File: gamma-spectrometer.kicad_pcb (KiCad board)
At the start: 2 copper layers, 123.5 x 55 mm, 80 parts, among them J1 *, J2 *, J3 *, J4 *, J5 *, J6 *, Q1 2N7002, Q2 2N7002, Q3 MMBT5088LT1G, Q4 MMBT5088LT1G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

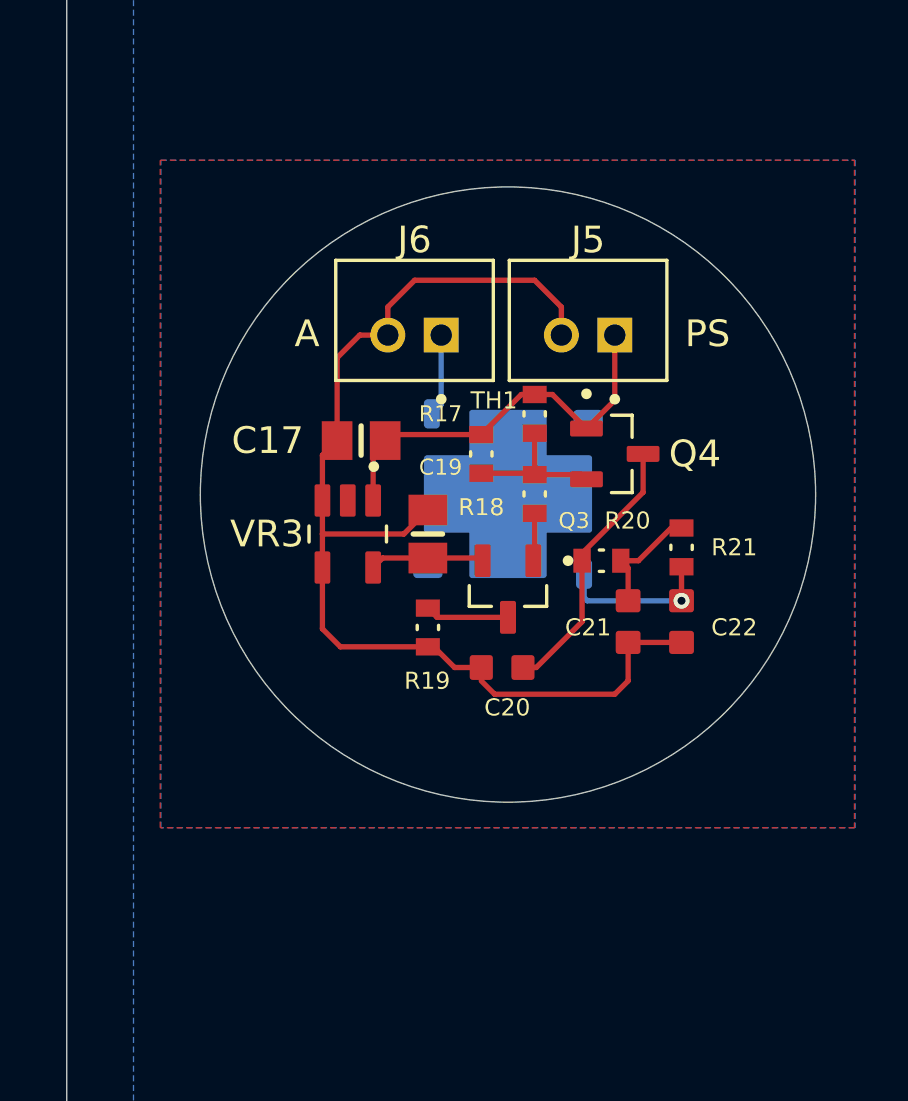
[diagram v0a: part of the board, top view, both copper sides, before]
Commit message: Corrected labels
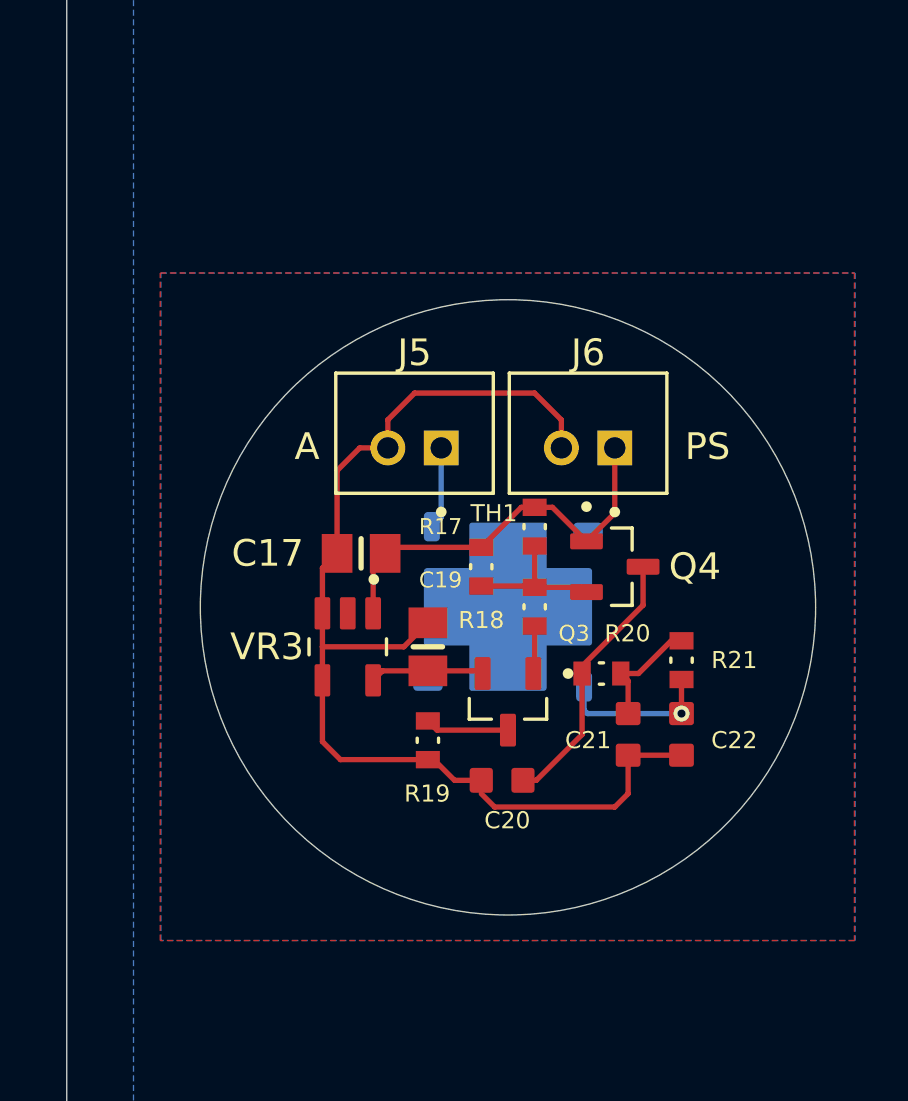
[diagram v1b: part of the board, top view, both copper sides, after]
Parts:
- moved C17 4.22 mm to (194.5, 82.2)
- moved C19 4.22 mm to (197.0, 85.7)
- moved C20 4.22 mm to (199.8, 90.7)
- moved C21 4.22 mm to (204.5, 89.0)
- moved C22 4.22 mm to (206.5, 89.0)
- moved J5 4.22 mm to (196.5, 77.7)
- moved J6 4.22 mm to (203.0, 77.7)
- moved Q3 4.22 mm to (200.0, 87.8)
- moved Q4 4.22 mm to (204.0, 82.7)
- moved R17 4.22 mm to (199.0, 82.7)
- moved R18 4.22 mm to (201.0, 84.2)
- moved R19 4.22 mm to (197.0, 89.2)
- moved R20 4.22 mm to (203.5, 86.7)
- moved R21 4.22 mm to (206.5, 86.2)
- moved TH1 4.22 mm to (201.0, 81.2)
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- renumbered J6 to J5, J5 to J6
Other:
- outline, holes or cut-outs redrawn

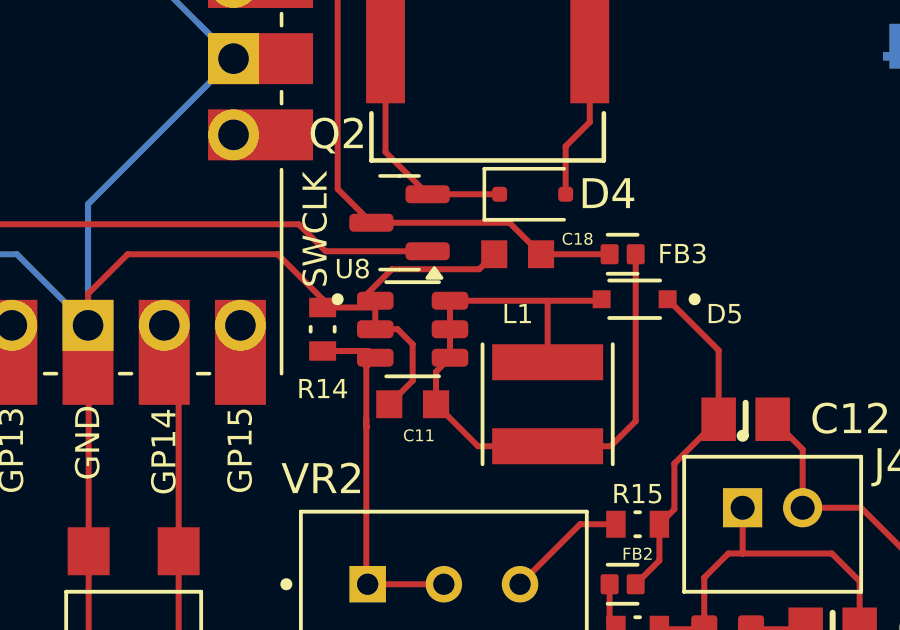
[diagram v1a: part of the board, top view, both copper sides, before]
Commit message: U8 5-6 pins connection error fix
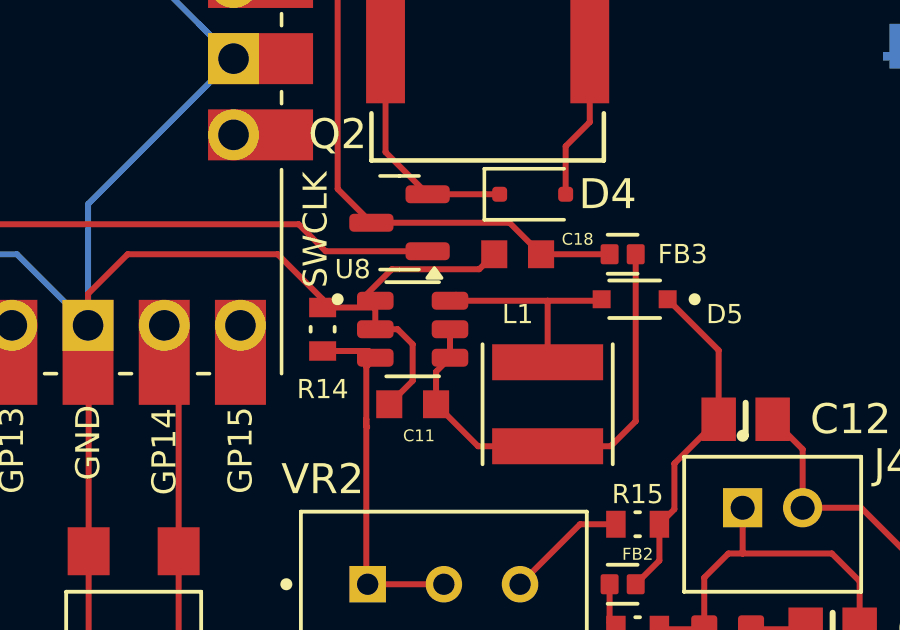
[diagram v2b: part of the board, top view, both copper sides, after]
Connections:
- C11 pad 1: Net-(D5-A) -> Net-(U8-VCC)
- FB3 pad 1: Net-(D5-A) -> Net-(U8-VCC)
- L1 pad 2: Net-(D5-A) -> Net-(U8-VCC)
- U8 pad 4: Net-(D5-A) -> Net-(U8-VCC)
- U8 pad 5: Net-(D5-A) -> Net-(U8-VCC)
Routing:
- net Net-(D5-A): track 25.5 -> 8.41 mm
- net Net-(U8-VCC): track 0.00 -> 16.1 mm
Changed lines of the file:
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@@
 	(net 86 "unconnected-(VR3-NC-Pad2)")
 	(net 87 "ANODE_OUT")
+	(net 88 "Net-(U8-VCC)")
 	(footprint "OPA357AIDBVR:SOT95P280X145-6N"
 		(layer "F.Cu")
@@
 			(layers "F.Cu" "F.Paste" "F.Mask")
 			(roundrect_rratio 0.125)
-			(net 70 "Net-(D5-A)")
+			(net 88 "Net-(U8-VCC)")
 			(pintype "passive")
 			(solder_mask_margin 0.102)
@@
 			(size 0.87 0.93)
 			(layers "F.Cu" "F.Paste" "F.Mask")
-			(net 70 "Net-(D5-A)")
+			(net 88 "Net-(U8-VCC)")
 			(pintype "passive")
 			(solder_mask_margin 0.102)
@@
 			(layers "F.Cu" "F.Paste" "F.Mask")
 			(roundrect_rratio 0.25)
-			(net 70 "Net-(D5-A)")
+			(net 88 "Net-(U8-VCC)")
 			(pinfunction "~{SHDN}")
 			(pintype "input")
@@
 			(layers "F.Cu" "F.Paste" "F.Mask")
 			(roundrect_rratio 0.25)
-			(net 70 "Net-(D5-A)")
+			(net 88 "Net-(U8-VCC)")
 			(pinfunction "VCC")
 			(pintype "power_in")
@@
 			(size 1.2 3.7)
 			(layers "F.Cu" "F.Paste" "F.Mask")
-			(net 70 "Net-(D5-A)")
+			(net 88 "Net-(U8-VCC)")
 			(pintype "passive")
 			(solder_mask_margin 0.102)
@@
 	)
 	(segment
-		(start 150.935 92)
-		(end 150.935 97.565)
-		(width 0.2)
-		(layer "F.Cu")
-		(net 70)
-	)
-	(segment
 		(start 148 93.55)
 		(end 149.75 93.55)
@@
 	)
 	(segment
-		(start 144.28 95.915)
-		(end 144.745 95.45)
-		(width 0.2)
-		(layer "F.Cu")
-		(net 70)
-	)
-	(segment
-		(start 145.68 98.4)
-		(end 144.28 97)
-		(width 0.2)
-		(layer "F.Cu")
-		(net 70)
-	)
-	(segment
-		(start 150.935 97.565)
-		(end 150.1 98.4)
-		(width 0.2)
-		(layer "F.Cu")
-		(net 70)
-	)
-	(segment
-		(start 144.745 95.45)
-		(end 145.05 95.45)
-		(width 0.2)
-		(layer "F.Cu")
-		(net 70)
-	)
-	(segment
 		(start 149.8 93.5)
 		(end 149.6 93.5)
@@
 	)
 	(segment
-		(start 150.1 98.4)
-		(end 145.68 98.4)
-		(width 0.2)
-		(layer "F.Cu")
-		(net 70)
-	)
-	(segment
-		(start 144.745 94.5)
-		(end 144.745 93.55)
-		(width 0.2)
-		(layer "F.Cu")
-		(net 70)
-	)
-	(segment
 		(start 148 95.6)
 		(end 148 93.55)
@@
 	)
 	(segment
-		(start 144.745 95.435)
-		(end 144.745 94.5)
-		(width 0.2)
-		(layer "F.Cu")
-		(net 70)
-	)
-	(segment
-		(start 144.28 97)
-		(end 144.28 95.915)
-		(width 0.2)
-		(layer "F.Cu")
-		(net 70)
-	)
-	(segment
 		(start 144.745 93.55)
 		(end 144.945 93.35)
@@
 	)
 	(segment
-		(start 144.73 95.45)
-		(end 144.745 95.435)
-		(width 0.2)
-		(layer "F.Cu")
-		(net 70)
-	)
-	(segment
 		(start 152.225 100.5)
 		(end 152.225 98.975)
@@
 		(net 87)
 	)
+	(segment
+		(start 150.935 92)
+		(end 150.935 97.565)
+		(width 0.2)
+		(layer "F.Cu")
+		(net 88)
+	)
+	(segment
+		(start 144.28 95.915)
+		(end 144.745 95.45)
+		(width 0.2)
+		(layer "F.Cu")
+		(net 88)
+	)
+	(segment
+		(start 145.68 98.4)
+		(end 144.28 97)
+		(width 0.2)
+		(layer "F.Cu")
+		(net 88)
+	)
+	(segment
+		(start 150.935 97.565)
+		(end 150.1 98.4)
+		(width 0.2)
+		(layer "F.Cu")
+		(net 88)
+	)
+	(segment
+		(start 144.745 95.45)
+		(end 145.05 95.45)
+		(width 0.2)
+		(layer "F.Cu")
+		(net 88)
+	)
+	(segment
+		(start 150.1 98.4)
+		(end 145.68 98.4)
+		(width 0.2)
+		(layer "F.Cu")
+		(net 88)
+	)
+	(segment
+		(start 144.745 95.435)
+		(end 144.745 94.5)
+		(width 0.2)
+		(layer "F.Cu")
+		(net 88)
+	)
+	(segment
+		(start 144.28 97)
+		(end 144.28 95.915)
+		(width 0.2)
+		(layer "F.Cu")
+		(net 88)
+	)
+	(segment
+		(start 144.73 95.45)
+		(end 144.745 95.435)
+		(width 0.2)
+		(layer "F.Cu")
+		(net 88)
+	)
 	(zone

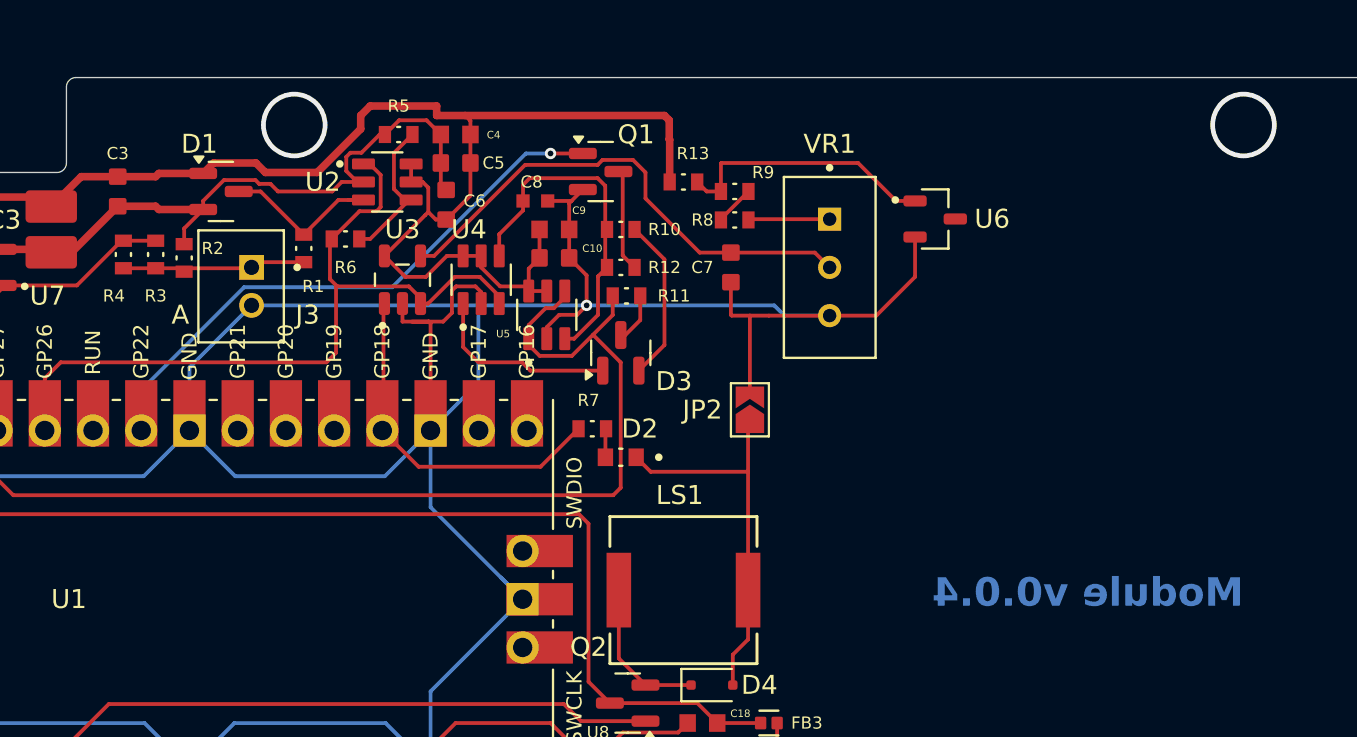
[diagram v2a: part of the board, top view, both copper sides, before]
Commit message: D1 1-2 pins conenction error fix
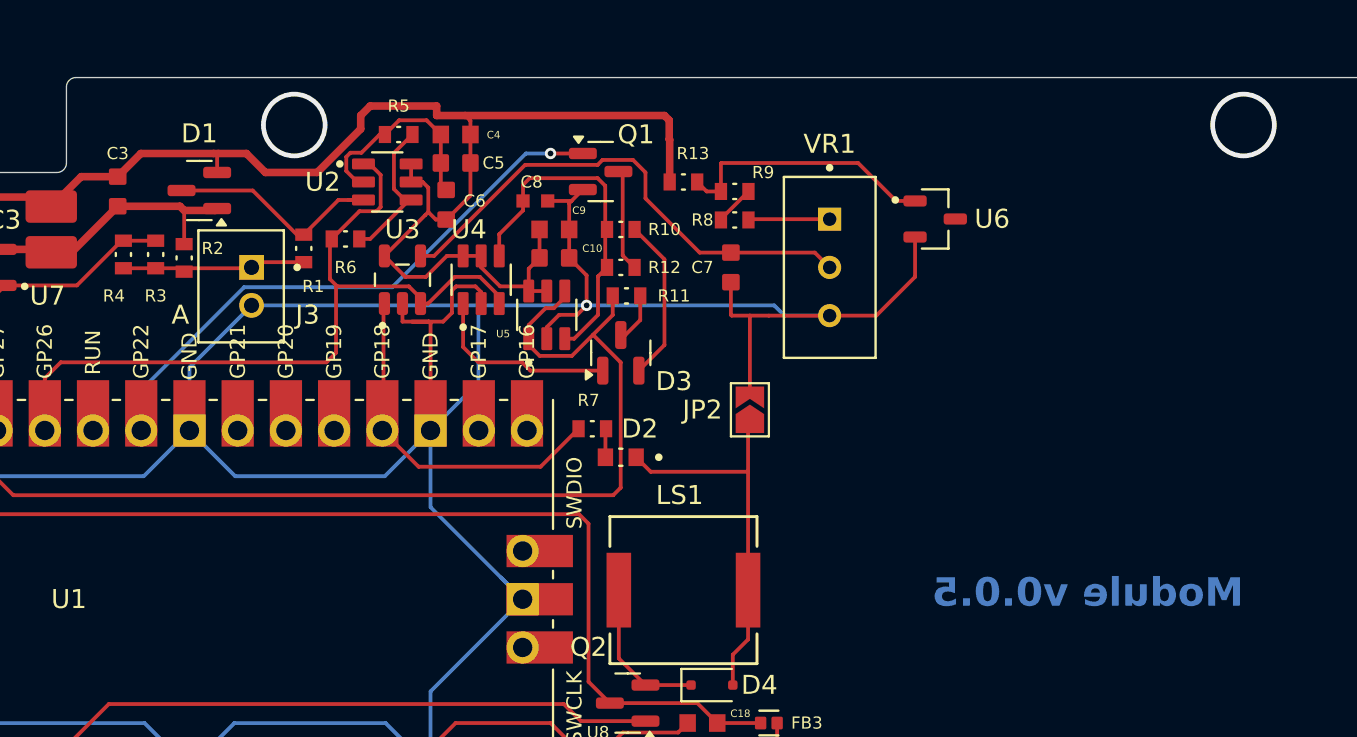
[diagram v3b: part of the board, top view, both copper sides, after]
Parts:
- moved D1 1.14 mm to (120.5, 64.0), turned to 180 degrees
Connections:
- D1 pad 1: VCC -> GND
- D1 pad 2: GND -> VCC
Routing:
- net GND: track 355.5 -> 346.4 mm
- net Net-(D1-COM): track 8.47 -> 11.5 mm
- net VCC: track 131.5 -> 133.0 mm
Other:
- board text added: "Module v0.0.5"
- board text removed: "Module v0.0.4"

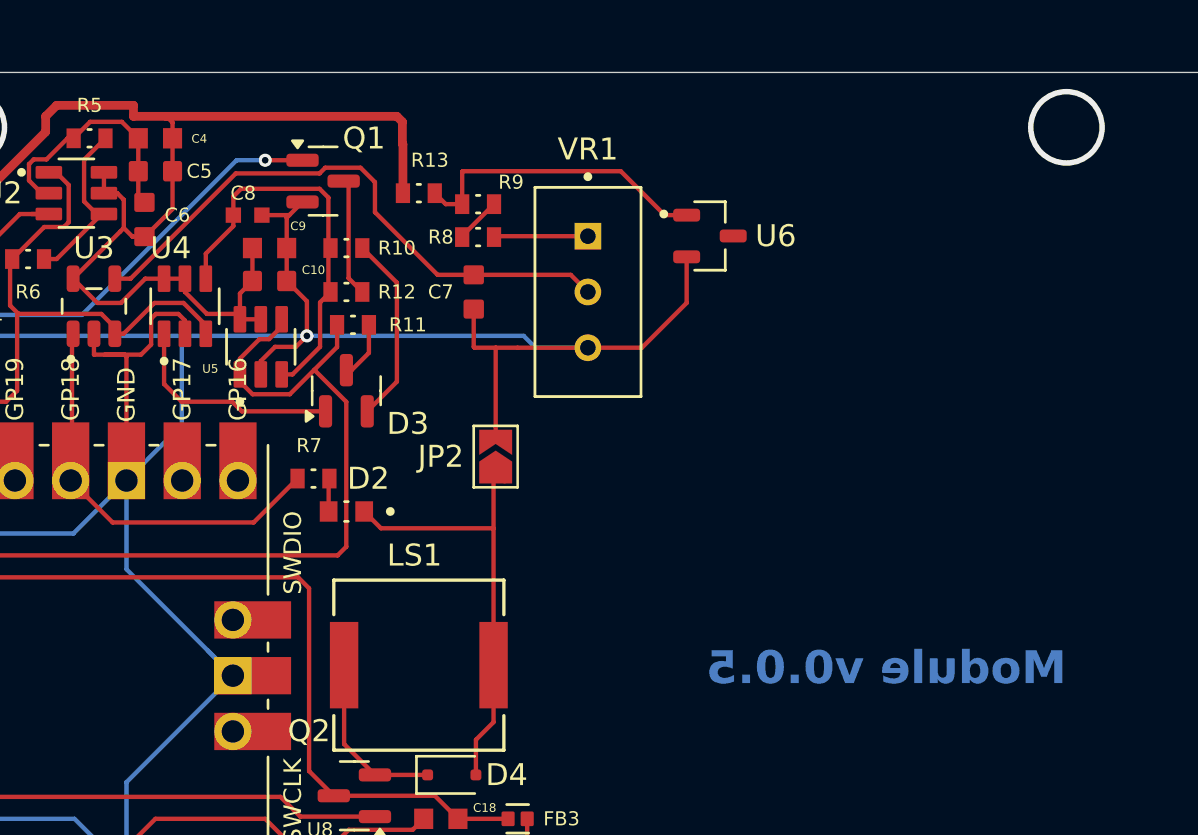
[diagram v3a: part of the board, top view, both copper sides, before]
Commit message: U2 GNS connection error fix
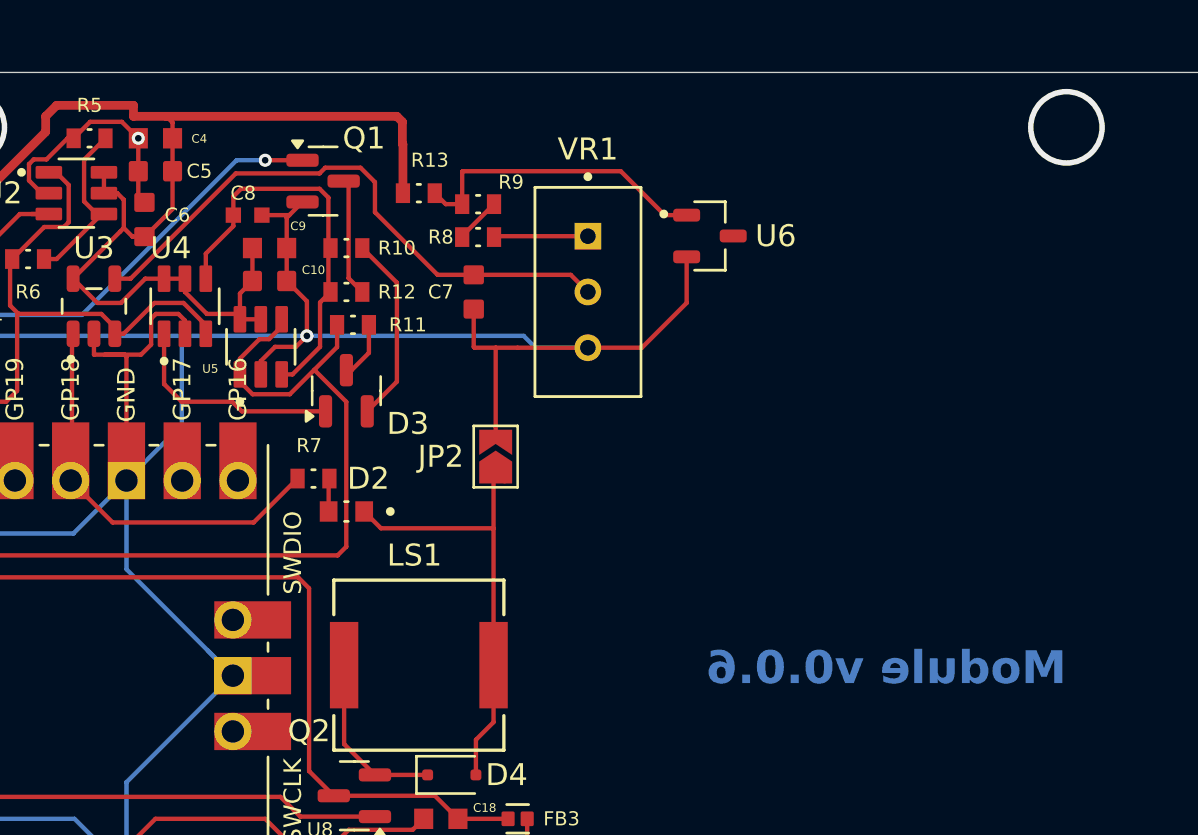
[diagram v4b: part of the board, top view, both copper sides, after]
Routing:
- net GND: vias 2 -> 3
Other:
- board text added: "Module v0.0.6"
- board text removed: "Module v0.0.5"
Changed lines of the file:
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@@
 		(layer "Edge.Cuts")
 	)
-	(gr_text "Module v0.0.5"
+	(gr_text "Module v0.0.6"
 		(at 175.5 86 0)
 		(layer "B.Cu" knockout)
@@
 		(net 17)
 	)
+	(via
+		(at 133.22 61)
+		(size 0.6)
+		(drill 0.3)
+		(layers "F.Cu" "B.Cu")
+		(net 17)
+	)
